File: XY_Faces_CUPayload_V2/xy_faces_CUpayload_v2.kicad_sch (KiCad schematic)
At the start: 26 parts, among them CN1 DF13A-5P-1.25H(21), CN2 DF13C-5P-1.25V(21), J2 Conn_01x01, J3 Conn_01x01, J4 Conn_01x01, J5 Conn_01x01, U1 VEML7700, U2 MCP9808_DFN, U3 DRV2605LDGS

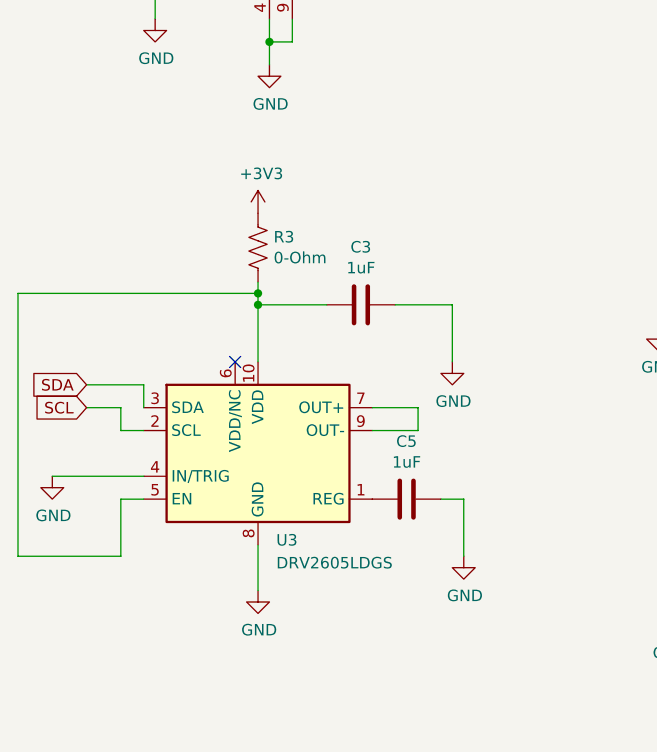
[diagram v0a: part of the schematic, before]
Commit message: Removed Magnetorquer/Driver and Modified Routing/Text
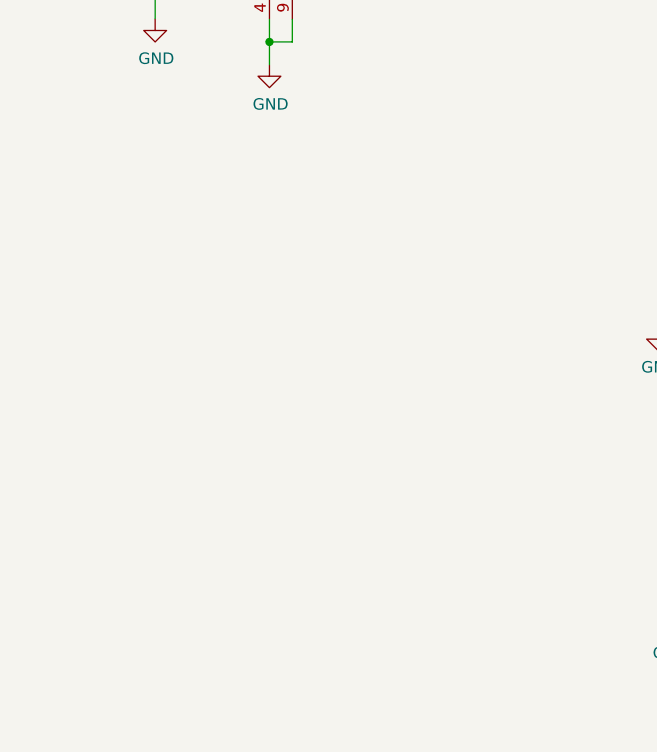
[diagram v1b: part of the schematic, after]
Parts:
- removed C3, C5: 1uF, Capacitor_SMD:C_0805_2012Metric, symbol Device:C
- removed R3: 0-Ohm, Resistor_SMD:R_0603_1608Metric, symbol Device:R_US
- removed U3: DRV2605LDGS, Package_SO:VSSOP-10_3x3mm_P0.5mm, symbol Driver_Haptic:DRV2605LDGS
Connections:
- no-connect marks 6 -> 5
